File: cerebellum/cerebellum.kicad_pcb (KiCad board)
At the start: 2 copper layers, 65 x 56 mm, 24 parts, among them J1 GPIO, J2 Conn_MOTA, J3 Conn_MOTB, J4 MD_POW, J5 Conn_SPI, J6 Conn_UART, J7 Conn_I2C, J8 VBUS(OUT), SW1 SW_PULLUP, SW2 SW_PULLDOWN, SW3 SW_SPDT, U2 POLOLU_TB6612_CARRIER, U3 HC-SR04

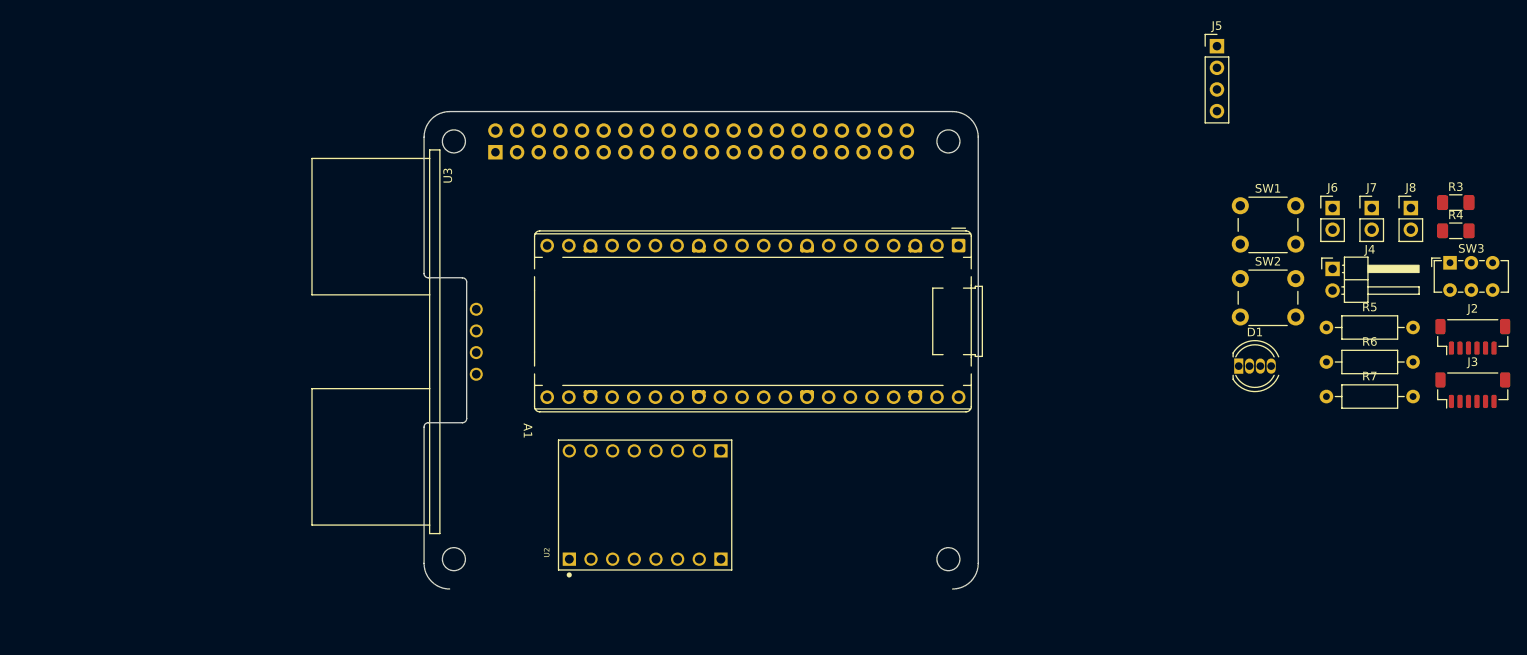
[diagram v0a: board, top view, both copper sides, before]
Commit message: update pcb
enlarge board
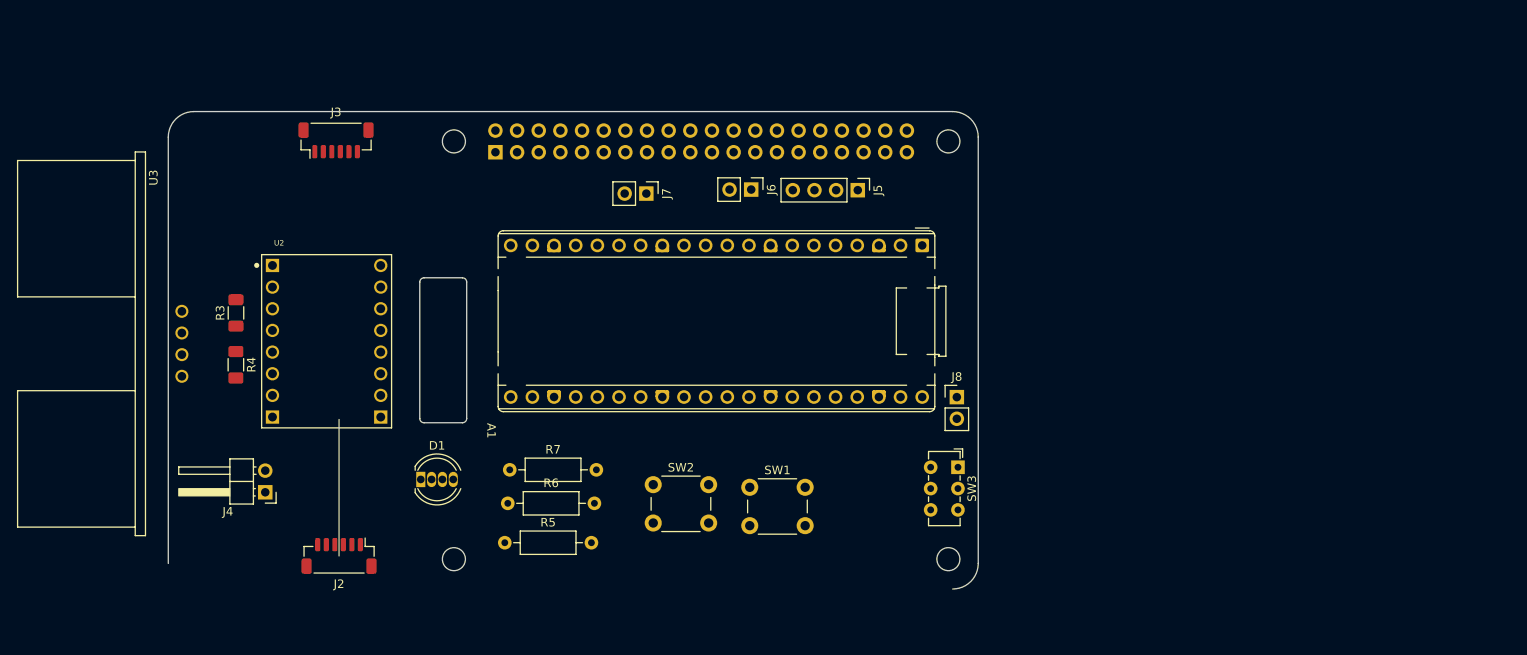
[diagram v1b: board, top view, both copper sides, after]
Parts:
- moved R4 143.9 mm to (77.9, 73.7), turned to -90 degrees
- moved R3 143.7 mm to (77.9, 67.6), turned to 90 degrees
- moved J3 136.5 mm to (89.7, 47.4)
- moved J2 135.4 mm to (90.0, 96.1), turned to 180 degrees
- moved J4 127.9 mm to (81.4, 88.7), turned to 180 degrees
- moved R5 99.6 mm to (109.5, 94.6)
- moved R6 97.4 mm to (109.8, 90.0)
- moved D1 96.9 mm to (99.6, 87.2)
- moved R7 96.2 mm to (110.0, 86.0)
- moved J7 85.1 mm to (126.1, 53.6), turned to -90 degrees
- moved SW2 73.0 mm to (126.9, 87.8)
- moved J6 68.2 mm to (138.4, 53.1), turned to -90 degrees
- moved SW1 66.3 mm to (138.2, 88.1)
- moved SW3 62.5 mm to (162.6, 85.7), turned to -90 degrees
- moved J8 57.7 mm to (162.5, 77.5)
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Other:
- board size 65 x 56 mm -> 95 x 56 mm

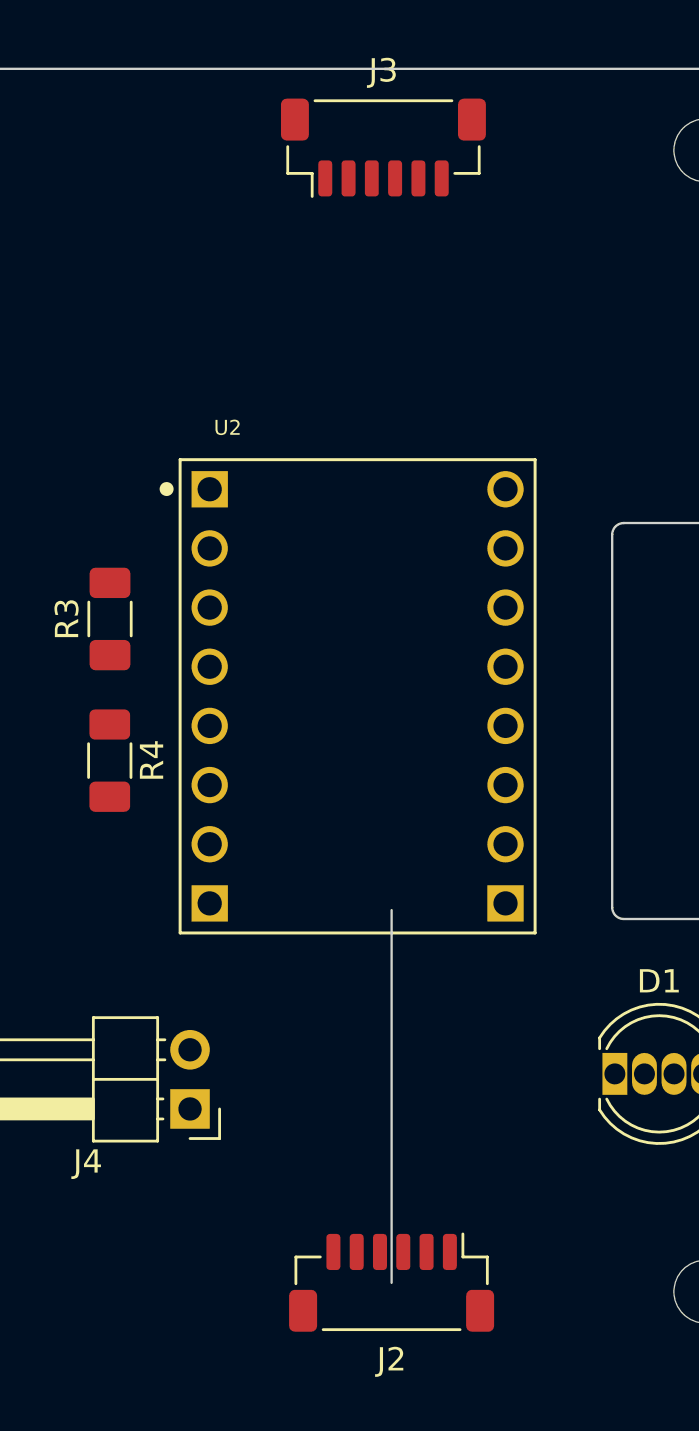
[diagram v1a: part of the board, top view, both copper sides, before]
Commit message: update md wiring
split motor a and b to two sides
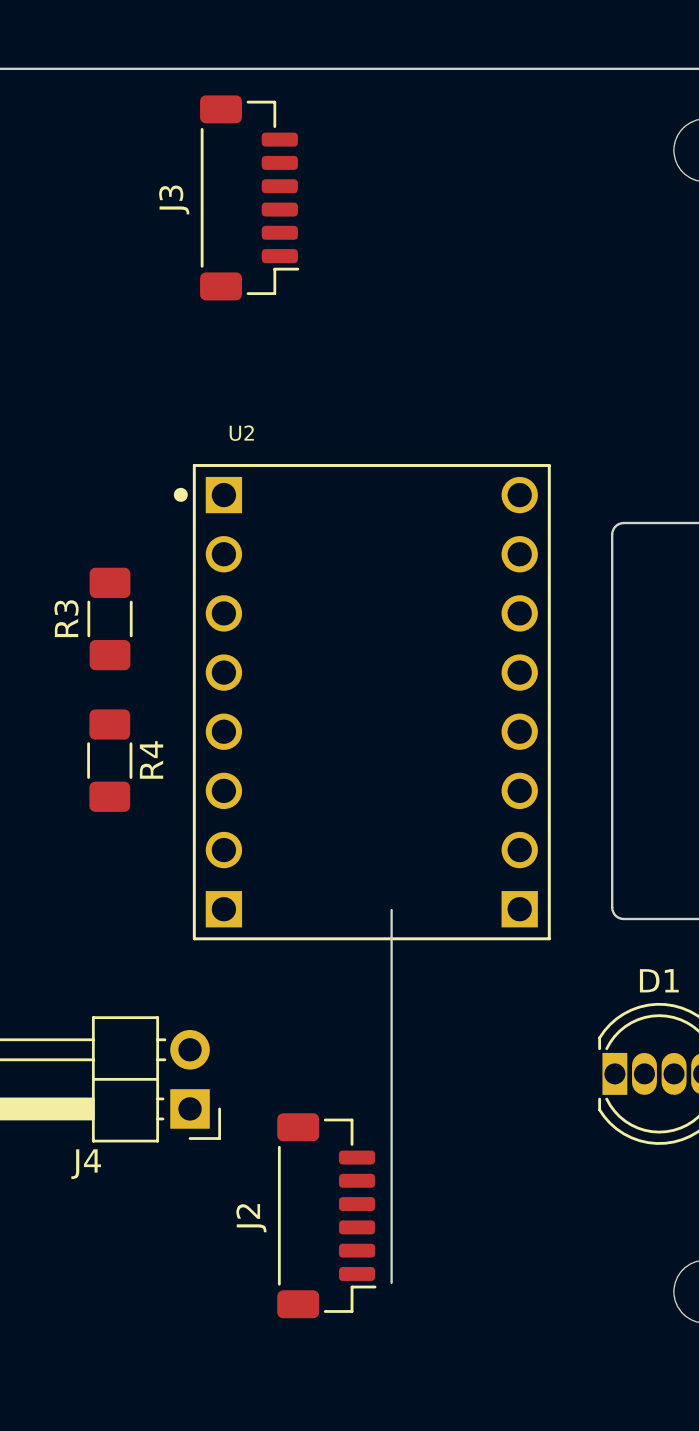
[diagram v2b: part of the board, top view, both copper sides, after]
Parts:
- moved J3 6.17 mm to (83.9, 49.5), turned to 90 degrees
- moved J2 4.02 mm to (87.2, 93.2), turned to 90 degrees
- moved U2 0.66 mm to (89.2, 71.2)
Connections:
- A1 pad 11: /SW_PD -> /SDA
- A1 pad 12: /SW_PU -> /SCL
- A1 pad 14: /SDA -> /AENC_Y
- A1 pad 15: /SCL -> /AENC_W
- A1 pad 16: /AENC_Y -> /STBY
- A1 pad 17: /AENC_W -> /PWMA
- A1 pad 19: /BENC_W -> /AIN2
- A1 pad 20: /BENC_Y -> /AIN1
- A1 pad 21: /PWMA -> /BIN1
- A1 pad 22: /AIN2 -> /BIN2
- A1 pad 24: /AIN1 -> /PWMB
- A1 pad 25: /STBY -> /BENC_Y
- A1 pad 26: /BIN1 -> /BENC_W
- A1 pad 27: /BIN2 -> /SW_PU
- A1 pad 29: /PWMB -> /SW_PD
- A1 pad 33: unconnected-(A1-AGND-Pad33) -> GND

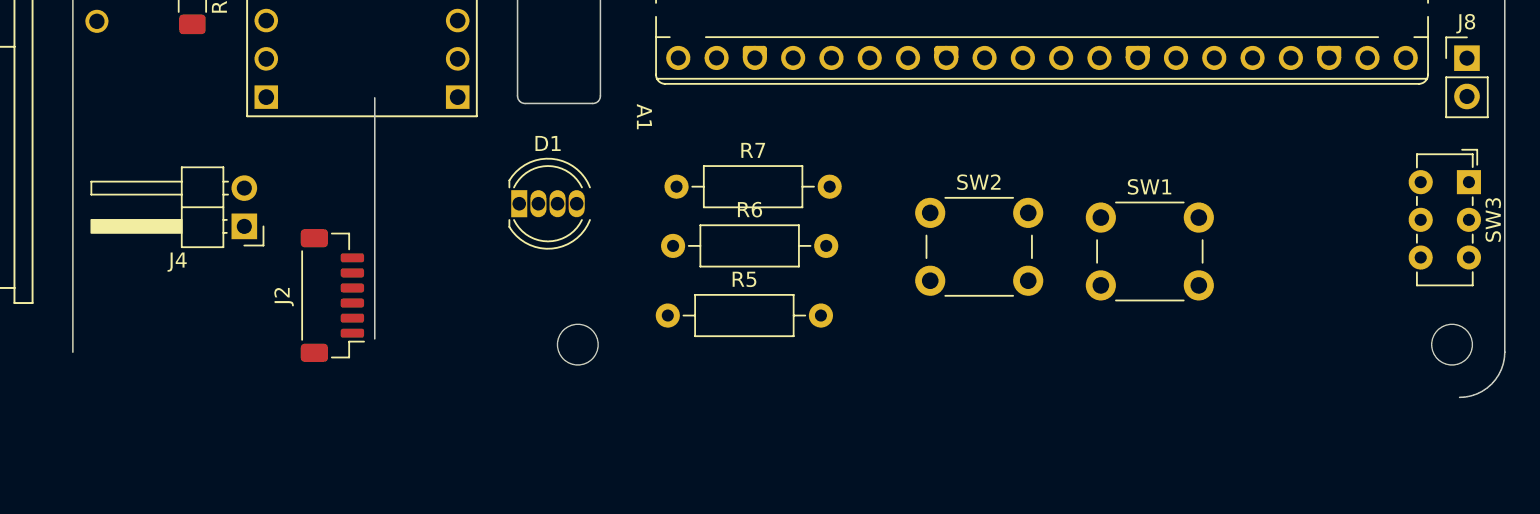
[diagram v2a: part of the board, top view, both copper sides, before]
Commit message: update pcb
use pcbway template
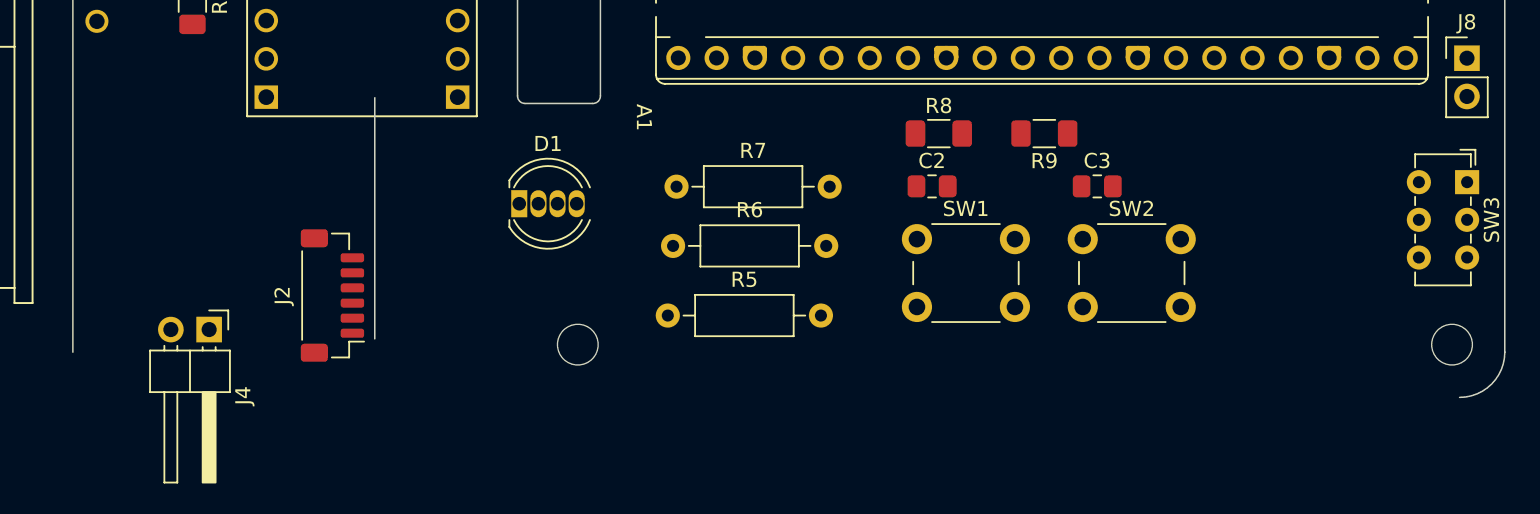
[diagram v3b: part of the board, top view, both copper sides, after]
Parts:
- added C2: 100n, Capacitor_SMD:C_0805_2012Metric_Pad1.18x1.45mm_HandSolder, F.Cu at (127.0, 86.0)
- added C3: 100n, Capacitor_SMD:C_0805_2012Metric_Pad1.18x1.45mm_HandSolder, F.Cu at (138.0, 86.0)
- added R8: 1k, Resistor_SMD:R_1206_3216Metric_Pad1.30x1.75mm_HandSolder, F.Cu at (127.5, 82.5)
- added R9: 1k, Resistor_SMD:R_1206_3216Metric_Pad1.30x1.75mm_HandSolder, F.Cu at (134.4, 82.5)
- moved SW1 12.3 mm to (126.0, 89.5)
- moved SW2 10.3 mm to (137.0, 89.5)
- moved J4 7.23 mm to (79.0, 95.5), turned to -90 degrees
- moved SW3 0.12 mm to (162.5, 85.7)
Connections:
- SW1 pad 1: PICO3.3 -> /SW_PU
- SW1 pad 2: /SW_PU -> GND
- SW2 pad 1: GND -> PICO3.3
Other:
- copper layers 2 -> 4
- board text removed: "DISPLAY (OPTIONAL)"
- board text removed: "Extend PCB edge 0.5mm if using SMT header"
- board text removed: "PoE"
- board text removed: "RJ45"
- board text removed: "USB"

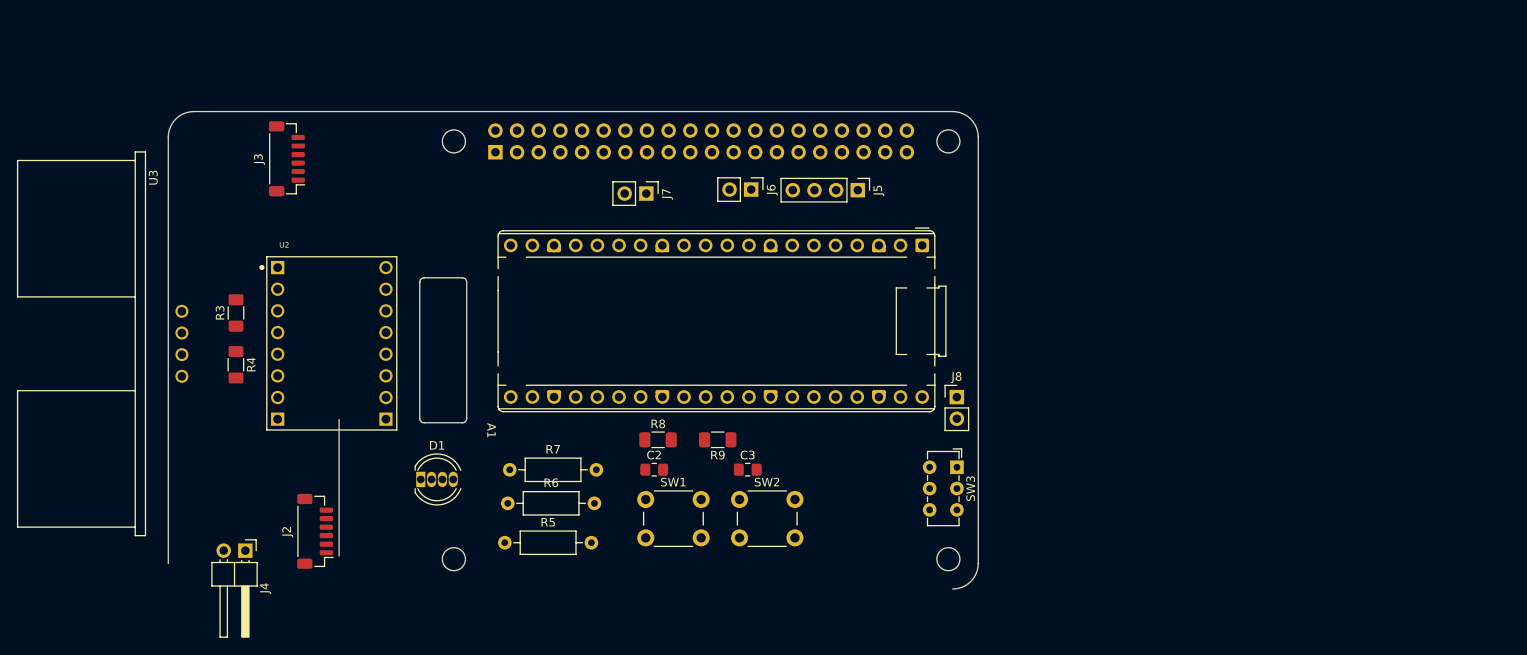
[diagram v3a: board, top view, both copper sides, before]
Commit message: update design
wire up
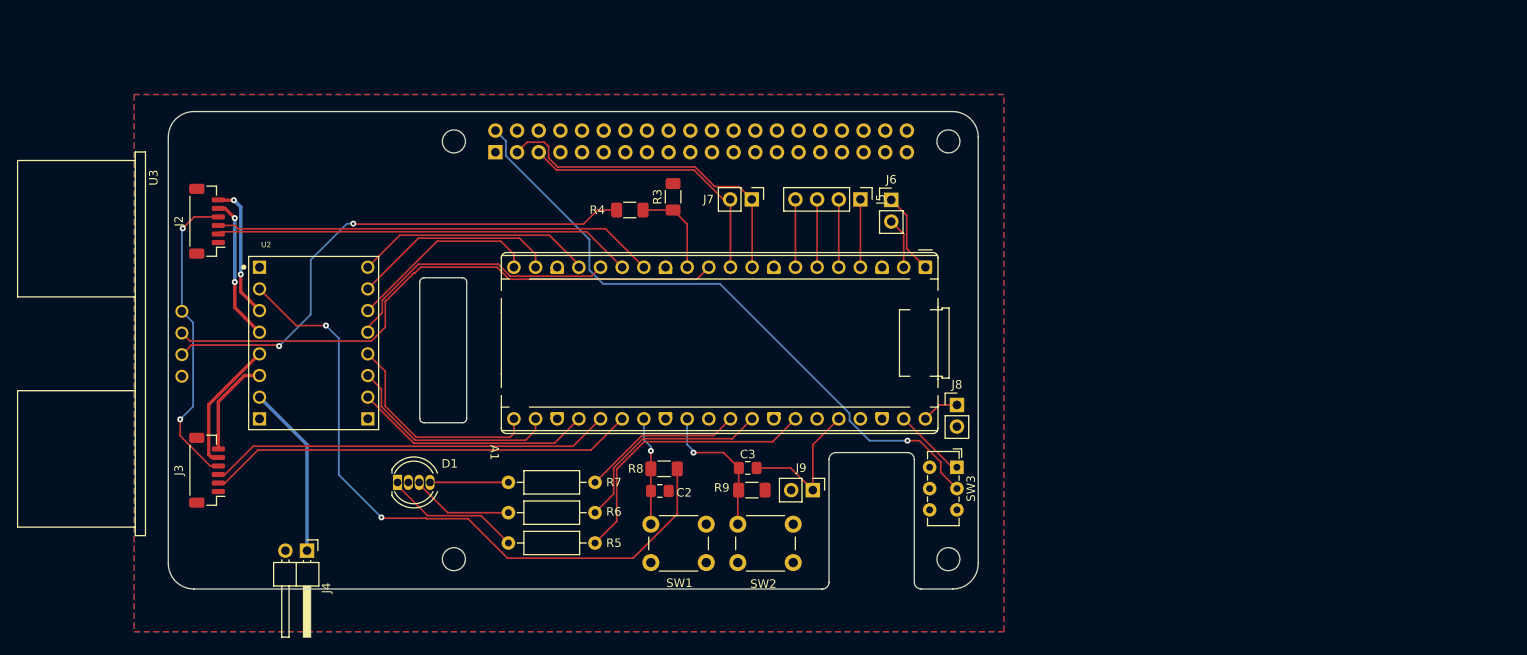
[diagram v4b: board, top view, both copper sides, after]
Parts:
- added J9: 3V3(OUT), Connector_PinHeader_2.54mm:PinHeader_1x02_P2.54mm_Vertical, F.Cu at (145.6, 88.4)
- moved R3 53.0 mm to (129.2, 54.0)
- moved R4 49.6 mm to (124.1, 55.5), turned to 180 degrees
- moved J2 38.5 mm to (74.5, 56.9)
- moved J3 37.7 mm to (74.5, 86.1)
- moved J6 16.5 mm to (154.8, 54.4), turned to 0 degrees
- moved J7 12.4 mm to (138.4, 54.3)
- moved SW2 9.72 mm to (143.3, 96.9), turned to 180 degrees
- moved J4 7.23 mm to (86.3, 95.5)
- moved R9 7.13 mm to (138.4, 88.4)
- moved R8 3.47 mm to (128.2, 85.9)
- moved SW1 2.96 mm to (126.6, 92.4)
- moved D1 2.75 mm to (96.9, 87.5)
- moved A1 2.59 mm to (158.8, 62.3)
- moved C2 2.58 mm to (127.7, 88.5)
- moved U2 2.13 mm to (87.0, 71.2)
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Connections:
- A1 pad 1: /TRIG -> /UART0_TX
- A1 pad 10: /UART0_RX -> /SCL
- A1 pad 11: /SDA -> /TRIG
- A1 pad 12: /SCL -> /ECHO
- A1 pad 2: /ECHO -> /UART0_RX
- A1 pad 9: /UART0_TX -> /SDA
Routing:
- net +5V: track 0.00 -> 112.1 mm, vias 0 -> 3
- net PICO3.3: track 0.00 -> 96.2 mm, vias 0 -> 2
- net /TRIG: track 0.00 -> 68.7 mm
- net Net-(U3-ECHO): track 0.00 -> 61.9 mm, vias 0 -> 2
- net /AENC_Y: track 0.00 -> 51.9 mm
- net /BENC_W: track 0.00 -> 50.5 mm
- net /AENC_W: track 0.00 -> 49.2 mm
- net /BENC_Y: track 0.00 -> 47.5 mm
- net /SDA: track 0.00 -> 39.5 mm
- net /R_LED: track 0.00 -> 33.1 mm
- net /STBY: track 0.00 -> 32.8 mm
- net /SCL: track 0.00 -> 32.7 mm
- net /PWMB: track 0.00 -> 28.2 mm
- net /PWMA: track 0.00 -> 28.1 mm
- net /BIN2: track 0.00 -> 25.8 mm
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- added copper zone on B.Cu, net GND
- added copper zone on F.Cu, net GND
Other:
- outline, holes or cut-outs redrawn

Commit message: update pcb
add labels
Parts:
- added G***: LOGO, LOGO, F.Cu at (87.4, 49.4)
- D1: value LED_RKGB -> RKGB
- J2: value Conn_MOTA -> MOTA
- J3: value Conn_MOTB -> MOTB
- POW: renamed from SW3; value SW_SPDT -> on
- moved J6 4.00 mm to (158.8, 54.3), turned to -90 degrees
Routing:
- net +5V: track 112.1 -> 152.8 mm
- net /UART0_RX: track 5.96 -> 7.96 mm
- net /UART0_TX: track 9.56 -> 7.96 mm
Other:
- board text added: "+"
- board text added: "-"
- board text added: "3V3"
- board text added: "3V3(OUT)"
- board text added: "AIN1"
- board text added: "AIN2"
- board text added: "AO1"
- board text added: "AO2"
- board text added: "B"
- board text added: "BIN1"
- board text added: "BIN2"
- board text added: "BO1"
- board text added: "BO2"
- board text added: "G"
- board text added: "GND"
- board text added: "I2C1_SCL"
- board text added: "I2C1_SDA"
- board text added: "K"
- board text added: "Micro-USB"
- board text added: "PWMA"
- board text added: "PWMB"
- board text added: "R"
- board text added: "R1 DiffDriver Carrier V2025.04"
- board text added: "RX0"
- board text added: "RaspberryPi Pico"
- board text added: "SPI0_CSn"
- board text added: "SPI0_RX"
- board text added: "SPI0_SCK"
- board text added: "SPI0_TX"
- board text added: "STBY"
- board text added: "SW_D"
- board text added: "SW_U"
- board text added: "TB6612FNG"
- board text added: "TX0"
- board text added: "VBUS"
- board text added: "VMOT"
- board text added: "W"
- board text added: "Y"
- board text added: "off"

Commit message: generate gerbers
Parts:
- J5 SPI: renamed from J5
- J6 UART: renamed from J6
- J7 I2C: renamed from J7
- OFF POW ON: renamed from POW
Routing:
- net PICO3.3: track 96.2 -> 115.1 mm
- net +5V: track 152.8 -> 154.6 mm
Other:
- board text added: "5V(OUT)"
- board text added: "CSn0"
- board text added: "GP0"
- board text added: "GP15"
- board text added: "GP16"
- board text added: "SCK0"
- board text added: "SCL1"
- board text added: "SDA1"
- board text added: "SRX0"
- board text added: "STX0"
- board text removed: "3V3(OUT)"
- board text removed: "I2C1_SCL"
- board text removed: "I2C1_SDA"
- board text removed: "SPI0_CSn"
- board text removed: "SPI0_RX"
- board text removed: "SPI0_SCK"
- board text removed: "SPI0_TX"
- board text removed: "off"
